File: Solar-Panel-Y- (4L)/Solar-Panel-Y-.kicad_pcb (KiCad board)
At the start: 4 copper layers, 64 x 58 mm, 87 parts, among them J1 FTS-107-01-X-DV-A, J2 BM02B-SRSS-TB, Q1 NX3008NBKS, Q2 MBT2222ADW1T1, Q3 NX3008NBKS, Q4 MBT2222ADW1T1, SW1 D2F-L2-A1, SW2 D2F-L2-A, U1 BQ25570RGRR, U2 OPT4001, U3 MAX40200AUK

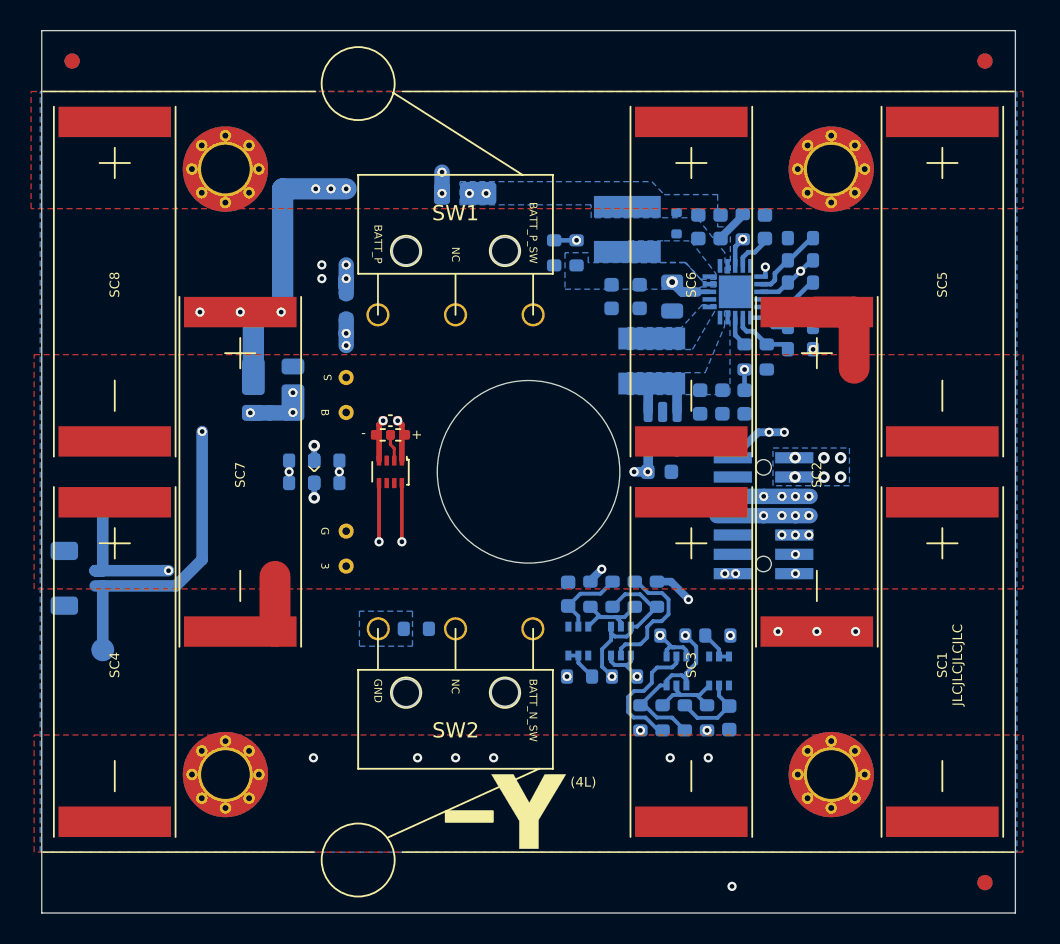
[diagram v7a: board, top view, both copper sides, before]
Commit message: Moved -Y switches out 1mm
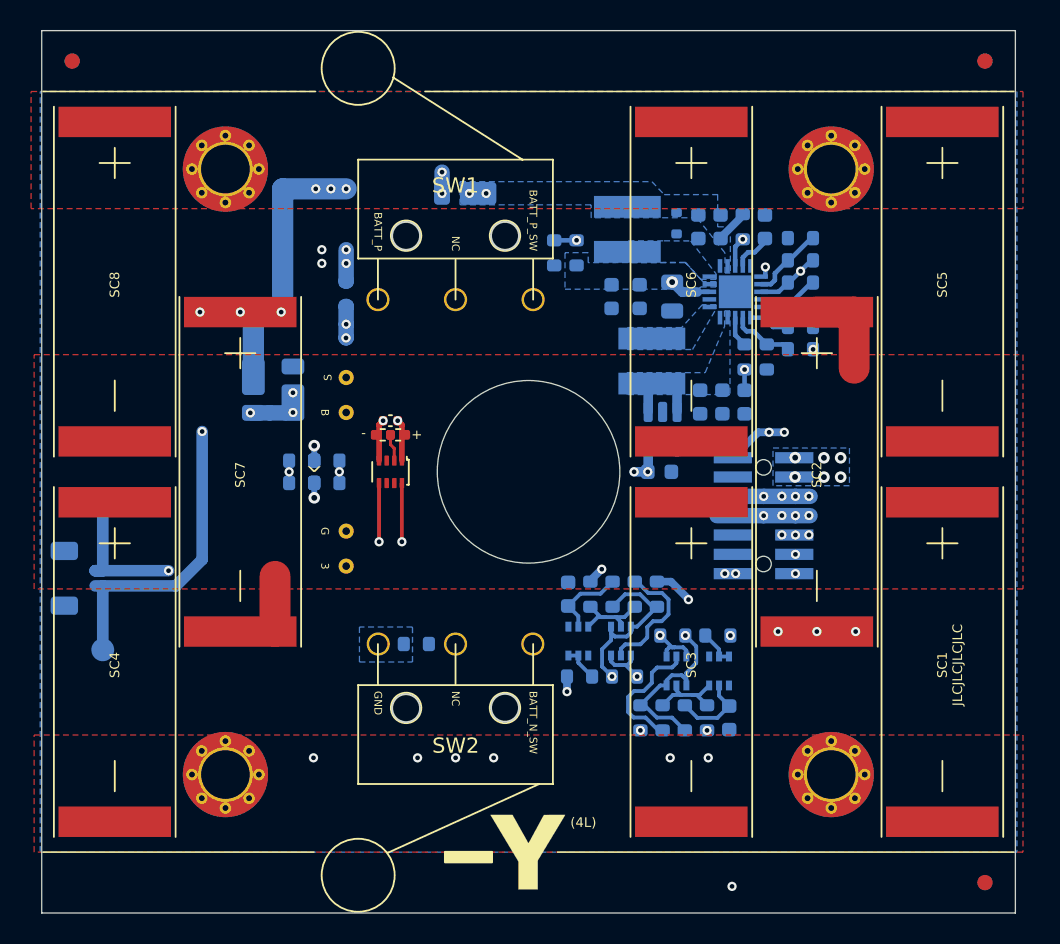
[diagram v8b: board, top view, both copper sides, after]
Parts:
- moved Ref** 2.67 mm to (122.0, 89.9)
- moved SW2 1.00 mm to (100.2, 75.3)
- moved SW1 1.00 mm to (100.2, 52.7)
- moved R31 1.00 mm to (97.6, 75.3)
- moved R3 0.83 mm to (93.0, 52.3)
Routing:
- net +3V3: track 8.94 -> 9.94 mm
